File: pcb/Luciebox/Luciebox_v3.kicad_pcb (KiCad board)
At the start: 2 copper layers, 100 x 100 mm, 71 parts, among them J4 Screw_Terminal_01x07, J5 Screw_Terminal_01x07, J7 USB_B_Mini, P1 CONN_01X01, P2 CONN_01X01, P3 CONN_01X01, P4 CONN_01X01, P5 Digital, P6 Power, P7 Digital, P8 Analog, Q2 N-Channel_Mosfet, SW10 Switch_tilt, SW11 Switch_tilt, SW12 Switch_tilt, SW9 Switch_tilt, T1 terminal_3x1, T13 terminal_8x1, T2 terminal_8x1, T3 terminal_8x1, T4 terminal_3x1, T5 terminal_3x1, T6 terminal_3x1, T8 terminal_3x1, T9 terminal_8x1, U1 CA56-12SRWA, U3 ATmega328-PU, U4 8X8PADS, Y1 16MHz

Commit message: pcb work on button pcb
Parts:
- H1, H2, H3, H4, H5, H6, H7, H8: footprint MountingHole:MountingHole_4mm -> Luciebox:MountingHole_4.3mm_M4
- moved R1 10.5 mm to (55.8, 80.0)
- moved T1 9.06 mm to (64.9, 71.4)
- moved T4 9.06 mm to (64.9, 75.4)
- moved S2 7.32 mm to (73.0, 83.1)
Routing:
- net Net-(J4-Pad5): track 51.8 -> 49.0 mm
- net /1(Tx): track 50.1 -> 48.2 mm
- net /13(SCK): track 58.2 -> 57.3 mm

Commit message: before finishing v3
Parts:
- moved T13 80.4 mm to (57.6, 72.8)
- moved R49 58.5 mm to (27.0, 59.2), turned to 270 degrees
- moved H7 52.6 mm to (50.0, 95.5)
- moved T2 26.1 mm to (55.1, 68.2)
- moved T3 25.0 mm to (55.1, 65.7)
- moved R1 22.5 mm to (38.5, 65.5), turned to 180 degrees
- moved T9 11.7 mm to (57.6, 75.3), turned to 0 degrees
- moved T1 9.55 mm to (71.9, 64.9)
- moved T4 9.55 mm to (71.9, 68.9)
- moved J7 9.25 mm to (100.0, 15.7)
- moved T8 9.25 mm to (96.9, 26.3)
- moved D1 9.25 mm to (86.1, 20.6)
- moved U4 8.59 mm to (90.7, 40.4)
- moved H6 6.83 mm to (95.5, 65.5)
- moved H8 6.67 mm to (95.5, 75.5)
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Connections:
- T13 pad 1: /0(Rx) -> /A3
- T13 pad 2: /8 -> /1(Tx)
- T13 pad 3: /12(MISO) -> /4
- T13 pad 5: /7 -> /0(Rx)
- T13 pad 6: /A3 -> /8
- T13 pad 7: /1 -> /12(MISO)
- T13 pad 8: /4 -> /7
- T2 pad 1: /0(Rx) -> GND
- T2 pad 2: /1 -> VCC_minimalCurrent
- T2 pad 3: /13(SCK) -> /A1
- T2 pad 4: /12(MISO) -> Net-(R1-Pad1)
- T2 pad 5: Net-(R1-Pad1) -> /0(Rx)
- T2 pad 6: VCC_minimalCurrent -> /8
- T2 pad 7: GND -> /12(MISO)
- T2 pad 8: /A2 -> /7
- T3 pad 1: /0(Rx) -> GND
- T3 pad 2: /1 -> VCC_minimalCurrent
- T3 pad 3: /13(SCK) -> /A2
- T3 pad 4: /12(MISO) -> Net-(R1-Pad1)
- T3 pad 5: Net-(R1-Pad1) -> /A3
- T3 pad 6: VCC_minimalCurrent -> /1(Tx)
- T3 pad 7: GND -> /4
- T3 pad 8: /A1 -> /13(SCK)
- U1 pad 5: /1 -> /1(Tx)
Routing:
- net GND: track 96.8 -> 401.9 mm, vias 4 -> 7
- net /A4(SDA): track 34.5 -> 127.6 mm, vias 0 -> 4
- net /A3: track 35.8 -> 124.1 mm, vias 0 -> 1
- net /1(Tx): track 48.2 -> 136.1 mm, vias 1 -> 3
- net /2: track 20.3 -> 92.4 mm, vias 0 -> 2
- net /A5(SCL): track 56.1 -> 126.3 mm, vias 1 -> 4
- net /A1: track 36.4 -> 95.0 mm
- net VCC_minimalCurrent: track 89.4 -> 142.1 mm, vias 1 -> 0
- net /0(Rx): track 94.0 -> 145.1 mm, vias 3 -> 4
- net /A2: track 34.6 -> 83.1 mm, vias 1 -> 0
- net /3(PWM): track 46.2 -> 93.3 mm, vias 0 -> 2
- net Net-(R1-Pad1): track 0.00 -> 43.3 mm
- net /A0: track 72.3 -> 113.8 mm, vias 0 -> 1
- net Net-(J4-Pad5): track 49.0 -> 90.3 mm, vias 1 -> 3
- net Net-(R46-Pad2): track 36.8 -> 0.00 mm, vias 1 -> 0
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- removed copper zone on B.Cu, net GND
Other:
- outline, holes or cut-outs redrawn
- board text added: "Luciebox v3.0 a nonkel Lode production 2020-12 luciebox.ameije.com"
- board text removed: "DAC_A3"
- board text removed: "LSB"
- board text removed: "Luciebox v2.0.0 a nonkel Lode production 2020-04-02. Blijde herinnering aan 1 jaar Lucie(box). www.ameije.com"
- board text removed: "MSB"
- board text removed: "PULL DOWN IF NC NOT AVAILABLE"

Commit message: pcb v3 comming along
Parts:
- removed J7: USB_B_Mini, Luciebox:usb_mini_Molex-0548190519
- added J1: USB_B_Mini, Luciebox:usb_mini_Molex-0548190519, F.Cu at (98.0, 15.3)
- added T10: terminal_3x1, Luciebox:Terminal_3x1_100mil, B.Cu at (53.9, 37.8)
- added T7: terminal_3x1, Luciebox:Terminal_3x1_100mil, B.Cu at (46.3, 37.8)
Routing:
- net GND: track 401.9 -> 420.8 mm
- net /13(SCK): track 77.2 -> 91.9 mm, vias 0 -> 1
- net /7: track 118.6 -> 132.7 mm, vias 3 -> 4
- net /A3: track 124.1 -> 137.1 mm, vias 1 -> 2
- net Net-(R5-Pad1): track 5.02 -> 18.0 mm
- net Net-(R4-Pad1): track 5.98 -> 18.9 mm
- net Net-(R3-Pad1): track 7.81 -> 20.2 mm
- net Net-(J4-Pad5): track 90.3 -> 101.7 mm
- net /0(Rx): track 145.1 -> 150.7 mm
- net Net-(J1-Pad2): track 9.23 -> 14.6 mm
- net /11(PWM-MOSI): track 72.5 -> 76.0 mm
- net Net-(J1-Pad3): track 17.1 -> 20.1 mm
- net /12(MISO): track 76.1 -> 79.2 mm
- net Net-(R2-Pad1): track 29.9 -> 32.8 mm
- net Net-(D1-Pad2): track 8.18 -> 5.36 mm
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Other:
- outline, holes or cut-outs redrawn

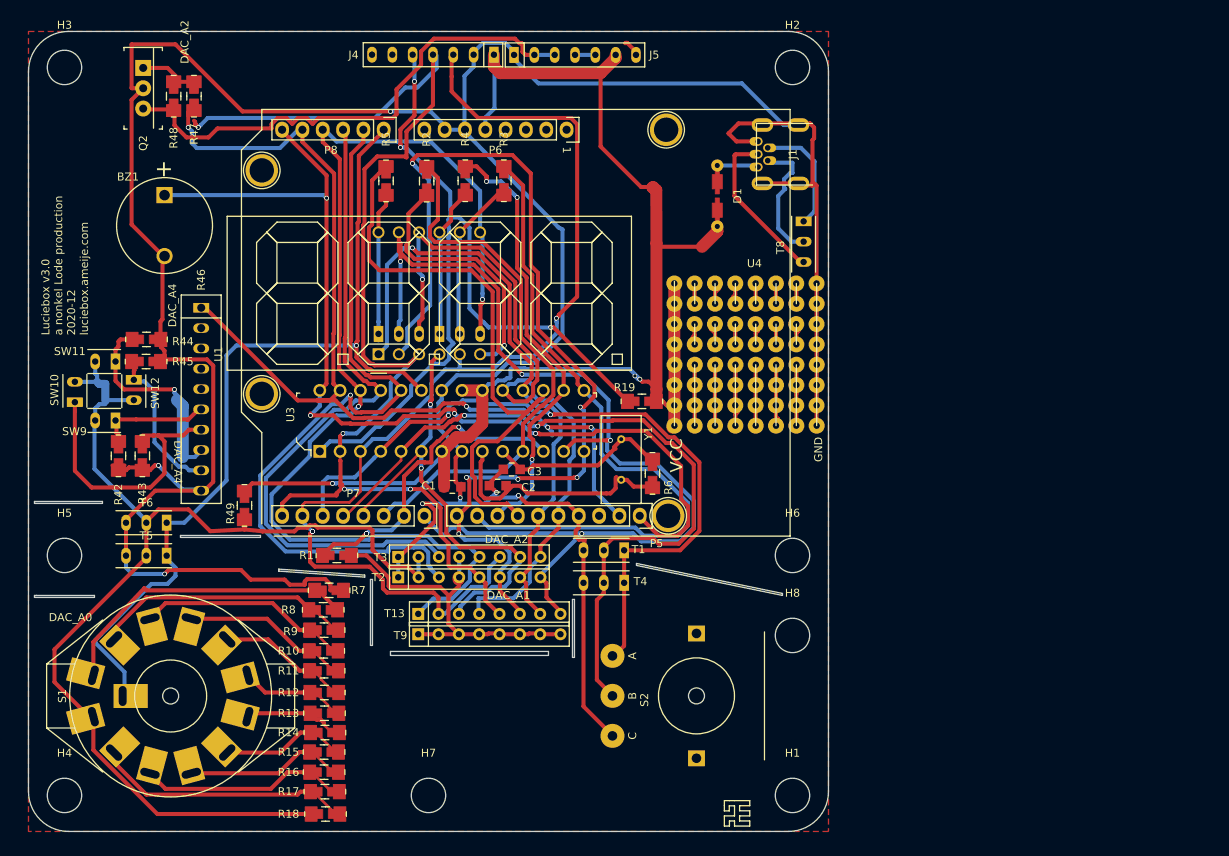
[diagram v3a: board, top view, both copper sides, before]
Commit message: published and ordered v3 luciebox v1 buttonboard. Gerbers included
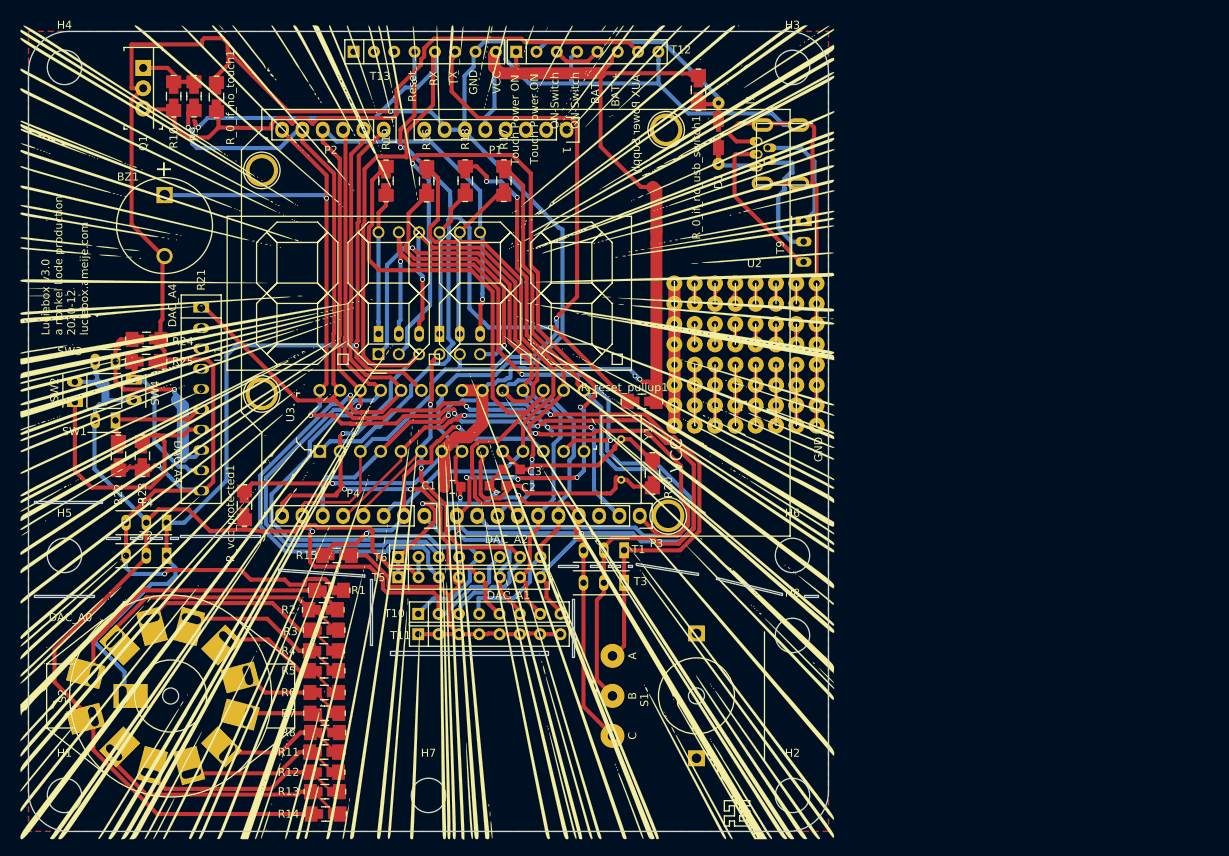
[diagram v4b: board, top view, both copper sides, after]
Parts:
- removed J4, J5: Screw_Terminal_01x07, Luciebox:Terminal_7x1_100mil
- added G***: LOGO, artwork:lines_burst, F.Cu at (49.8, 50.0)
- added G***: LOGO, artwork:wallpaper_abstract, B.Cu at (49.8, 50.4)
- added R_0_if_no_touch1: 0, Luciebox:1206_0805, F.Cu at (23.5, 8.20)
- added R_0_if_no_usb_switch1: 0, Luciebox:1206_0805, F.Cu at (83.8, 7.30)
- added T12: terminal_8x1, Luciebox:Terminal_8x1_100mil, F.Cu at (69.8, 2.54)
- added T13: terminal_8x1, Luciebox:Terminal_8x1_100mil, F.Cu at (49.5, 2.54)
- R9: renamed from R47; value 100K -> 10K
- moved D1 7.82 mm to (86.2, 12.8), turned to 90 degrees
- renumbered H4 to H1, H1 to H2, H2 to H3, H3 to H4, P6 to P1, P8 to P2, P5 to P3, P7 to P4, P1 to P5, P2 to P6, P3 to P7, P4 to P8, Q2 to Q1, R7 to R1, R48 to R10, R15 to R11, R16 to R12, R17 to R13, R18 to R14, R1 to R15, R2 to R16, R3 to R17, R4 to R18, R5 to R19, R8 to R2, R6 to R20, R46 to R21, R42 to R22, R43 to R23, R44 to R24, R45 to R25, R9 to R3, R10 to R4, R11 to R5, R12 to R6, R13 to R7, R14 to R8, R19 to R_reset_pullup1, R49 to R_vcc_protected1, S2 to S1, S1 to S2, SW9 to SW1, SW10 to SW2, SW11 to SW3, SW12 to SW4, T13 to T10, T9 to T11, T5 to T2, T4 to T3, T6 to T4, T2 to T5, T3 to T6, T10 to T8, T8 to T9, U4 to U2
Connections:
- D1 pad 1: VCC -> Net-(D1-Pad1)
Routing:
- net Net-(D1-Pad1): track 0.00 -> 29.4 mm
- net GND: track 420.8 -> 436.5 mm
- net Net-(Q1-Pad3): track 65.0 -> 76.8 mm
- net VCC: track 172.3 -> 178.7 mm
- net Net-(T12-Pad3): track 0.00 -> 6.08 mm
- net Net-(J5-Pad4): track 2.54 -> 0.00 mm
- net Net-(J5-Pad7): track 2.22 -> 0.00 mm
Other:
- outline, holes or cut-outs redrawn
